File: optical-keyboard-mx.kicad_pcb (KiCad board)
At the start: 2 copper layers, 324.8 x 186 mm, 413 parts, among them M1 LED, M10 LED, M11 LED, M12 LED, M13 LED, M14 LED, M15 LED, M16 LED, M17 LED, M18 LED, M19 LED, M2 LED, M20 LED, M21 LED, M22 LED, M23 LED, M24 LED, M25 LED, M26 LED, M27 LED, M28 LED, M29 LED, M3 LED, M30 LED, M31 LED, M32 LED, M33 LED, M34 LED, M35 LED, M36 LED, M37 LED, M38 LED, M39 LED, M4 LED, M40 LED, M41 LED, M42 LED, M43 LED, M44 LED, M45 LED, M46 LED, M47 LED, M48 LED, M49 LED, M5 LED, M50 LED, M51 LED, M52 LED, M53 LED, M54 LED, M55 LED, M56 LED, M57 LED, M58 LED, M59 LED, M6 LED, M60 LED, M61 LED, M62 LED, M63 LED, M64 LED, M65 LED, M66 LED, M67 LED, M68 LED, M69 LED, M7 LED, M70 LED, M71 LED, M72 LED, M73 LED, M74 LED, M8 LED, M9 LED, Q1 Q_Photo_NPN, Q10 Q_Photo_NPN, Q11 Q_Photo_NPN, Q12 Q_Photo_NPN, Q13 Q_Photo_NPN, Q14 Q_Photo_NPN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

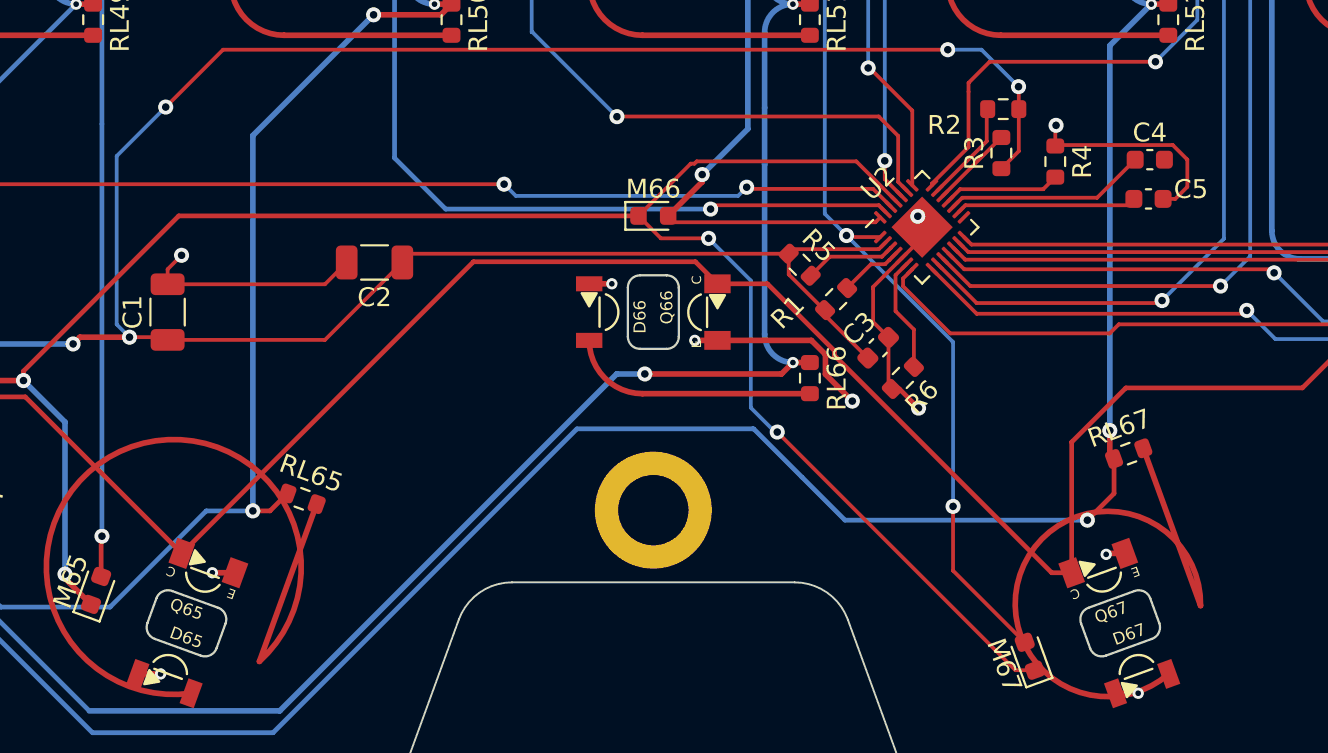
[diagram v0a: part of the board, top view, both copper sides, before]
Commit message: Reverse polarities of capacitor
M  jlcpcb/gerber/optical-keyboard-mx-B_Cu.gbl
M  jlcpcb/gerber/optical-keyboard-mx-B_Mask.gbs
M  jlcpcb/gerber/optical-keyboard-mx-B_Paste.gbp
M  jlcpcb/gerber/optical-keyboard-mx-B_Silkscreen.gbo
M  jlcpcb/gerber/optical-keyboard-mx-Edge_Cuts.gm1
M  jlcpcb/gerber/optical-keyboard-mx-F_Cu.gtl
M  jlcpcb/gerber/optical-keyboard-mx-F_Mask.gts
M  jlcpcb/gerber/optical-keyboard-mx-F_Paste.gtp
M  jlcpcb/gerber/optical-keyboard-mx-F_Silkscreen.gto
M  jlcpcb/gerber/optical-keyboard-mx-NPTH-drl_map.gbr
M  jlcpcb/gerber/optical-keyboard-mx-NPTH.drl
M  jlcpcb/gerber/optical-keyboard-mx-PTH-drl_map.gbr
M  jlcpcb/gerber/optical-keyboard-mx-PTH.drl
M  led_driver.kicad_sch
M  optical-keyboard-mx.kicad_pcb
M  optical-keyboard-mx.kicad_prl
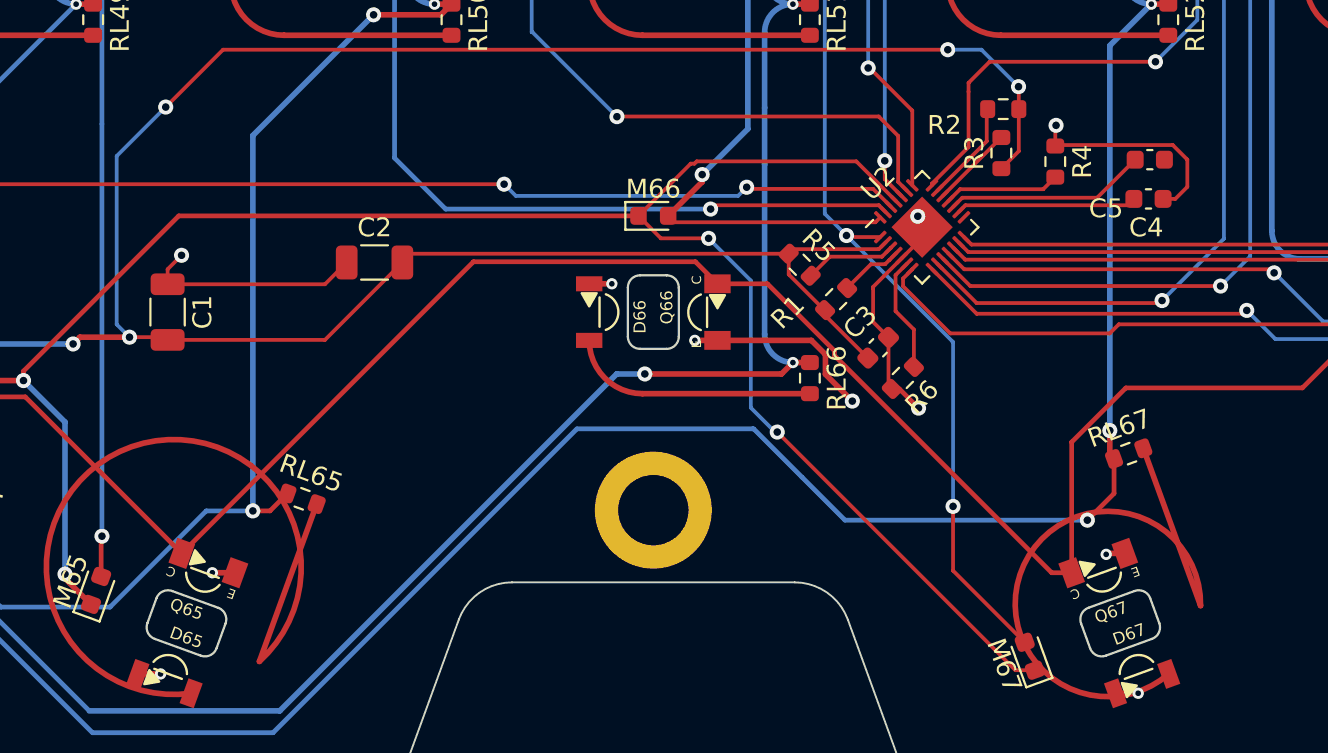
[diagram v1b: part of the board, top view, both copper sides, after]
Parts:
- turned C1 to -90 degrees
- turned C2 to 0 degrees
- turned C3 to -135 degrees
- turned C4 to 180 degrees
- turned C5 to 180 degrees
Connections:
- C1 pad 1: VCC -> GND
- C1 pad 2: GND -> VCC
- C2 pad 1: VCC -> GND
- C2 pad 2: GND -> VCC
- C3 pad 1: VCC -> GND
- C3 pad 2: GND -> VCC
- C4 pad 1: Net-(C4-Pad1) -> unconnected-(C4-Pad1)
- C4 pad 2: unconnected-(C4-Pad2) -> Net-(C4-Pad2)
- C5 pad 1: Net-(C5-Pad1) -> GND
- C5 pad 2: GND -> Net-(C5-Pad2)
- U2 pad 16: Net-(C5-Pad1) -> Net-(C5-Pad2)
- U2 pad 17: Net-(C4-Pad1) -> Net-(C4-Pad2)
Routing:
- net Net-(C4-Pad2): track 0.00 -> 10.7 mm
- net Net-(C4-Pad1): track 10.7 -> 0.00 mm
- net Net-(C5-Pad2): track 0.00 -> 9.58 mm
- net Net-(C5-Pad1): track 9.58 -> 0.00 mm

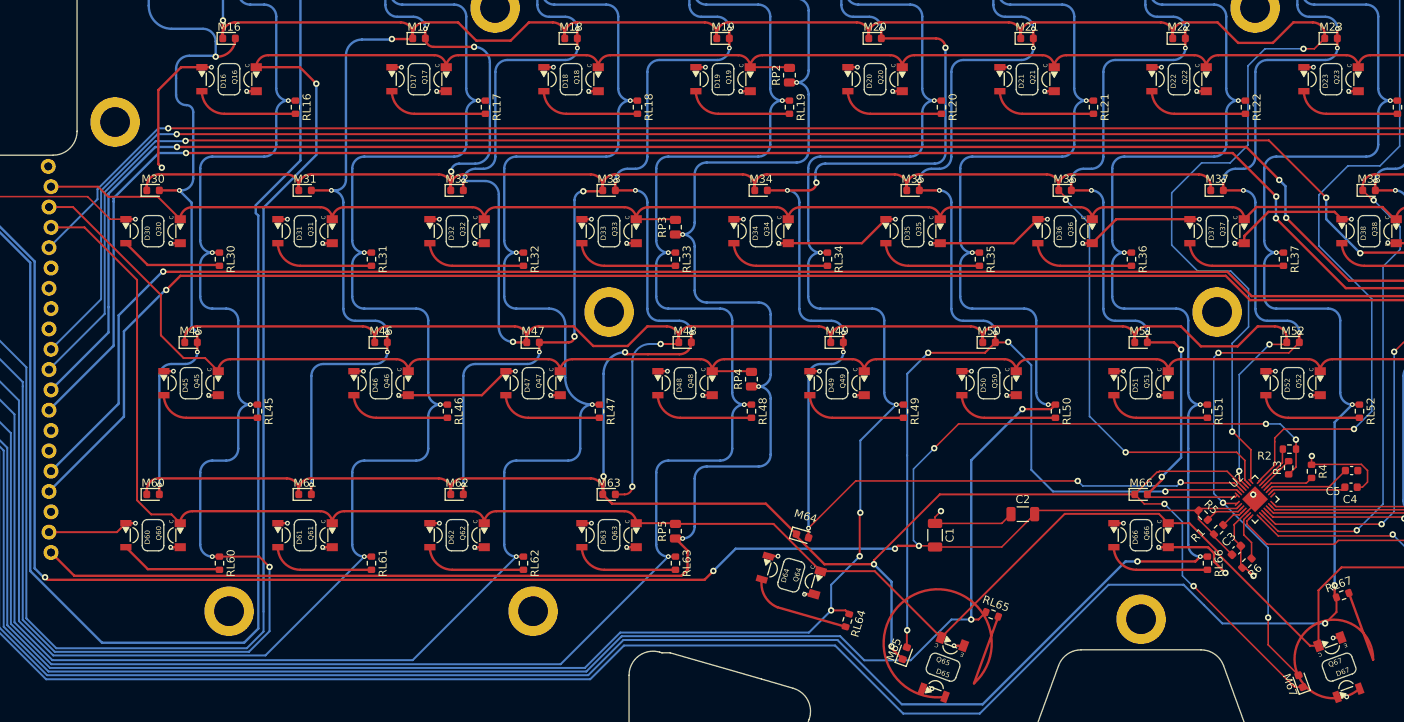
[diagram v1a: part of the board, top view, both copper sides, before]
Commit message: Fix bug where SCL SDA of I2c not connected
M  drawborder.py
M  led_driver.kicad_sch
M  optical-keyboard-mx.kicad_pcb
M  optical-keyboard-mx.kicad_prl
M  optical-keyboard-mx.kicad_sch
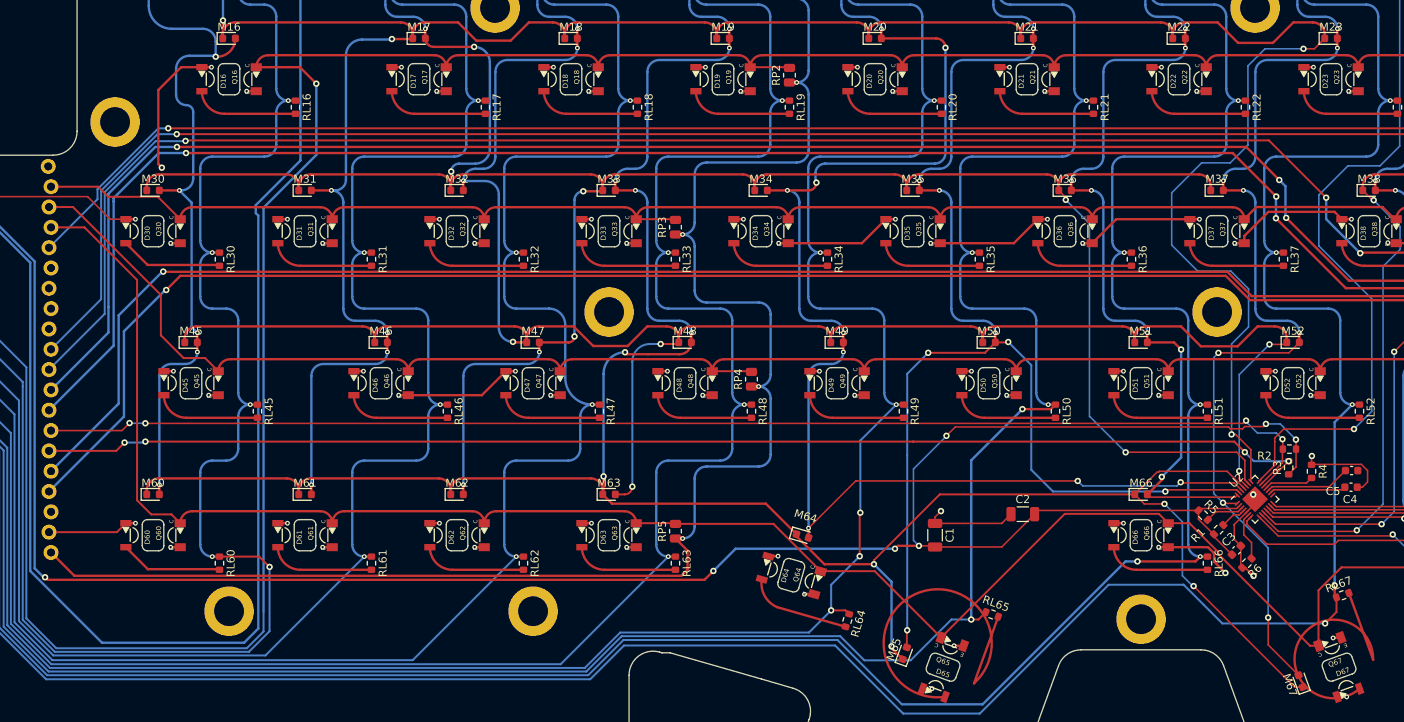
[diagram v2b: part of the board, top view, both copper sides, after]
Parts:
- RL1, RL10, RL11, RL12, RL13, RL14, RL15, RL16, RL17, RL18, RL19, RL2, RL20, RL21, RL22, RL23, RL24, RL25, RL26, RL27, RL28, RL29, RL3, RL30, RL31, RL32, RL33, RL34, RL35, RL36, RL37, RL38, RL39, RL4, RL40, RL41, RL42, RL43, RL44, RL45, RL46, RL47, RL48, RL49, RL5, RL50, RL51, RL52, RL53, RL54, RL55, RL56, RL57, RL58, RL59, RL6, RL60, RL61, RL62, RL63, RL64, RL65, RL66, RL67, RL68, RL69, RL7, RL70, RL71, RL72, RL73, RL74, RL8, RL9: value R_Led -> 560R
- RP1, RP2, RP3, RP4, RP5: value R_PT -> 6.8k
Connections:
- R2 pad 2: Net-(R2-Pad2) -> SCL
- R3 pad 2: Net-(R3-Pad2) -> SDA
- U1 pad 14: /SCL -> SCL
- U1 pad 15: /SDA -> SDA
- U2 pad 19: Net-(R3-Pad2) -> SDA
- U2 pad 20: Net-(R2-Pad2) -> SCL
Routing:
- net SCL: track 0.00 -> 162.2 mm, vias 0 -> 4
- net SDA: track 0.00 -> 160.8 mm, vias 0 -> 4
- net Net-(R2-Pad2): track 5.43 -> 0.00 mm
- net Net-(R3-Pad2): track 4.40 -> 0.00 mm
